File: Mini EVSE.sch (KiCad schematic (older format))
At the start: 33 parts, among them IC1 G3MC-201PL DC5, IC2 IRM-03-5, IC3 ATTINY84-20PU, IC4 RD-0512D, IC5 SI8261BAC-C-IP, J1 RE OUT, J10 M, J2 AC IN, J4 ICP, J5 SWITCH, J6 PILOTS, J7 M, J8 M, J9 M, X1 15.36MHz

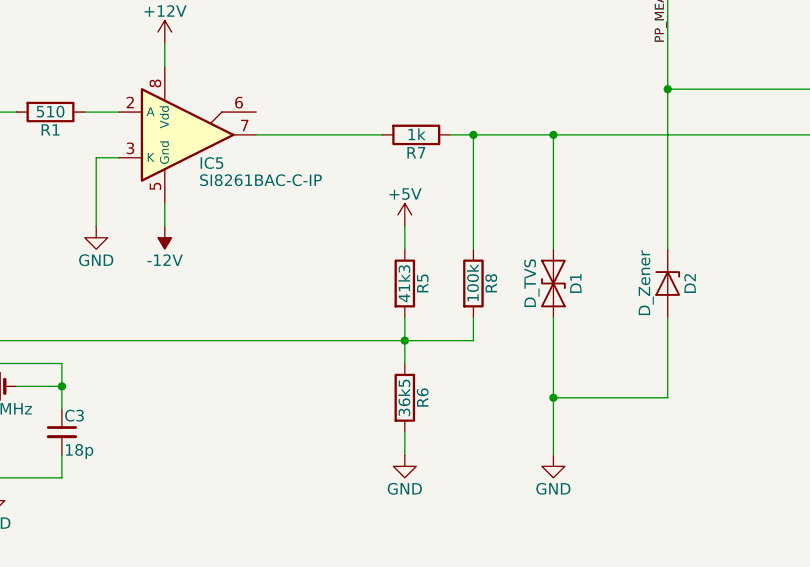
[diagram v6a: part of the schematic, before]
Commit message: Changed some pad sixes, component values
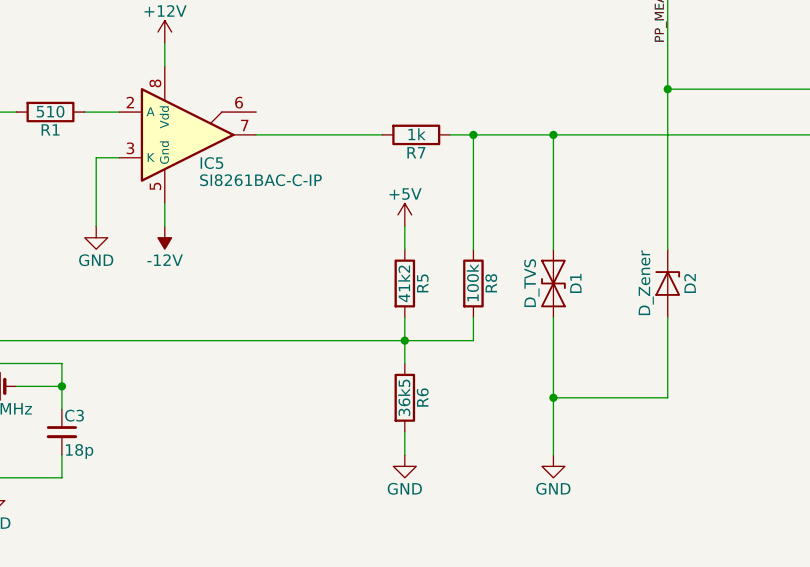
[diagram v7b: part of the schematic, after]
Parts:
- R5: value 41k3 -> 41k2
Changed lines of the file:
@@
 P 7450 3700
 F 0 "R5" V 7530 3700 50  0000 C CNN
-F 1 "41k3" V 7450 3700 50  0000 C CNN
+F 1 "41k2" V 7450 3700 50  0000 C CNN
 F 2 "Miscellaneous:R_Axial_DIN0207_L6.3mm_D2.5mm_P10.16mm_Horizontal" V 7380 3700 50  0001 C CNN
 F 3 "" H 7450 3700 50  0001 C CNN

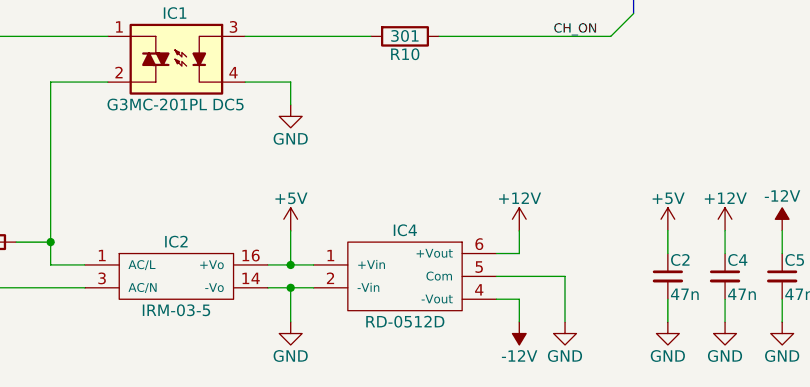
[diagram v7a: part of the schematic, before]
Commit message: Changed DC/DC converter to TMR1-0522
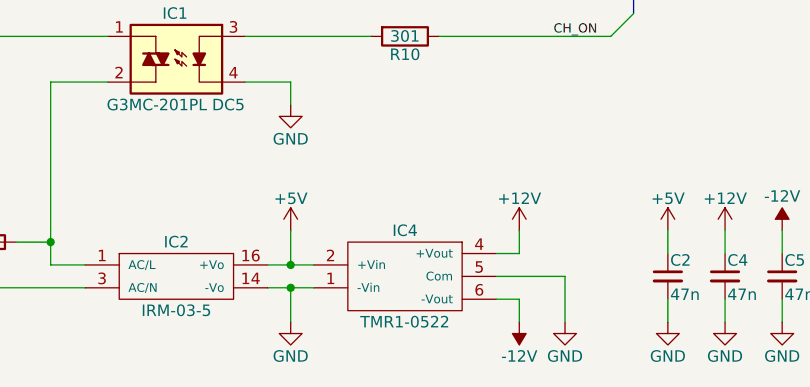
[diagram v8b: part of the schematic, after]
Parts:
- removed IC4: RD-0512D, Miscellaneous:Recom_1x05_Pitch2.54mm, symbol RD-0512D
- added IC4: TMR1-0522, symbol TMR1-0522
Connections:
- net +12V: now also IC4.4 (+Vout)
- net +5V: now also IC4.2 (+Vin)
- net -12V: now also IC4.6 (-Vout)
- net GND: now also IC4.1 (-Vin), IC4.5 (Com)
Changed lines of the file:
@@
-$EndComp
-$Comp
-L RD-0512D IC4
-U 1 1 59A6F2C8
-P 3850 6700
-F 0 "IC4" H 3850 6900 50  0000 C CNN
-F 1 "RD-0512D" H 3850 6500 50  0000 C CNN
-F 2 "Miscellaneous:Recom_1x05_Pitch2.54mm" H 3850 6700 50  0001 C CNN
-F 3 "" H 3850 6700 50  0001 C CNN
-	1    3850 6700
-	1    0    0    -1
 $EndComp
 $Comp
@@
 Wire Wire Line
 	7350 1650 7350 1750
+$Comp
+L TMR1-0522 IC4
+U 1 1 59B81475
+P 3850 6700
+F 0 "IC4" H 3850 6900 50  0000 C CNN
+F 1 "TMR1-0522" H 3850 6500 50  0000 C CNN
+F 2 "" H 3850 6700 50  0001 C CNN
+F 3 "" H 3850 6700 50  0001 C CNN
+	1    3850 6700
+	1    0    0    -1
+$EndComp
 $EndSCHEMATC
